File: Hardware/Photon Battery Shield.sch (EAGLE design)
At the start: 24 parts, among them U1 MAX1704X, U2 MCP73831

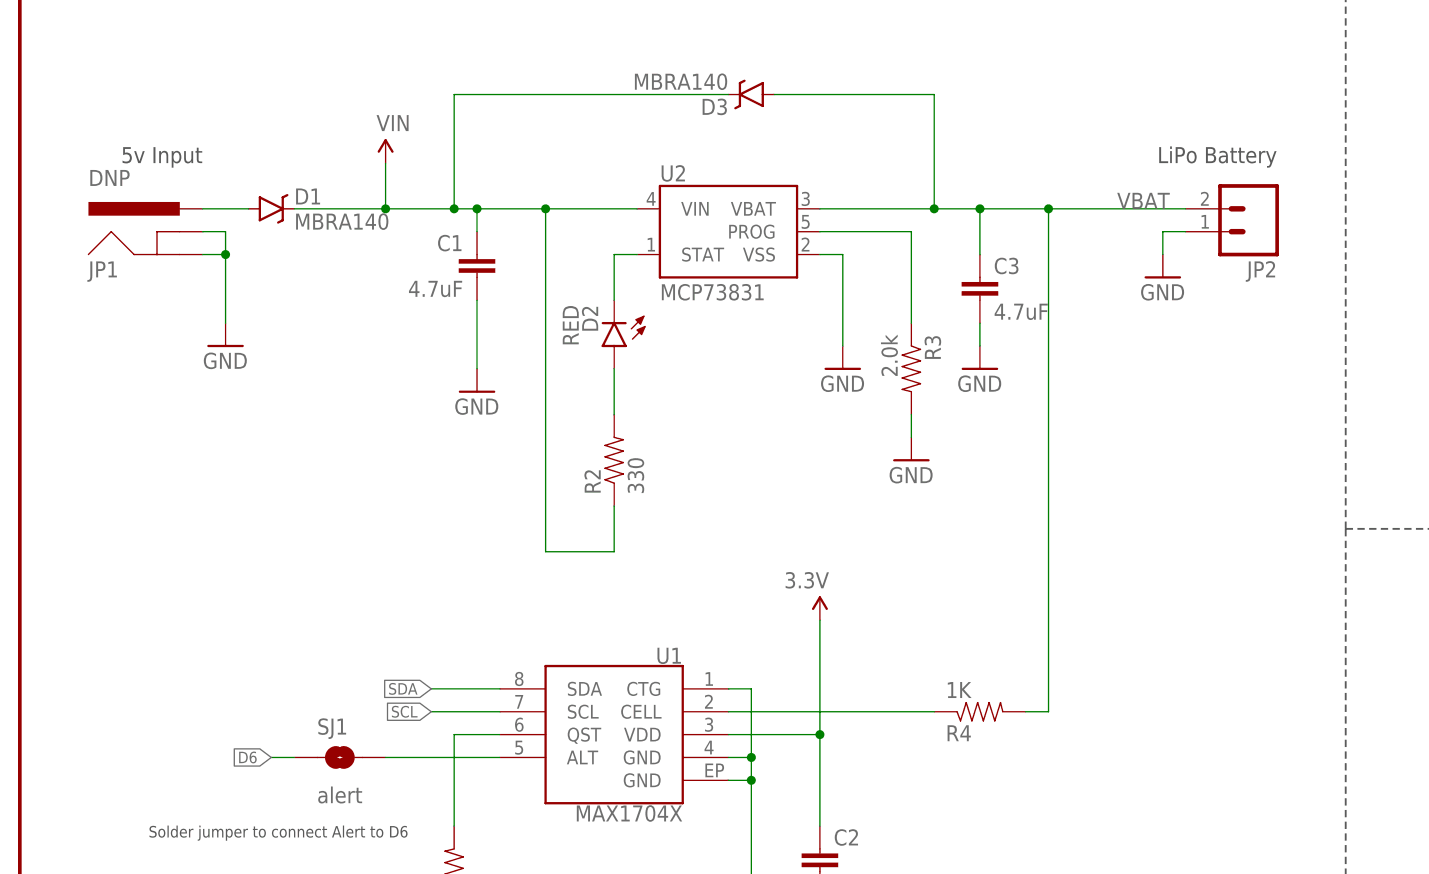
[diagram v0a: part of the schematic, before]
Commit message: Adding test point to VBAT. Reducing bSilk on barrel jack to avoid going over board.
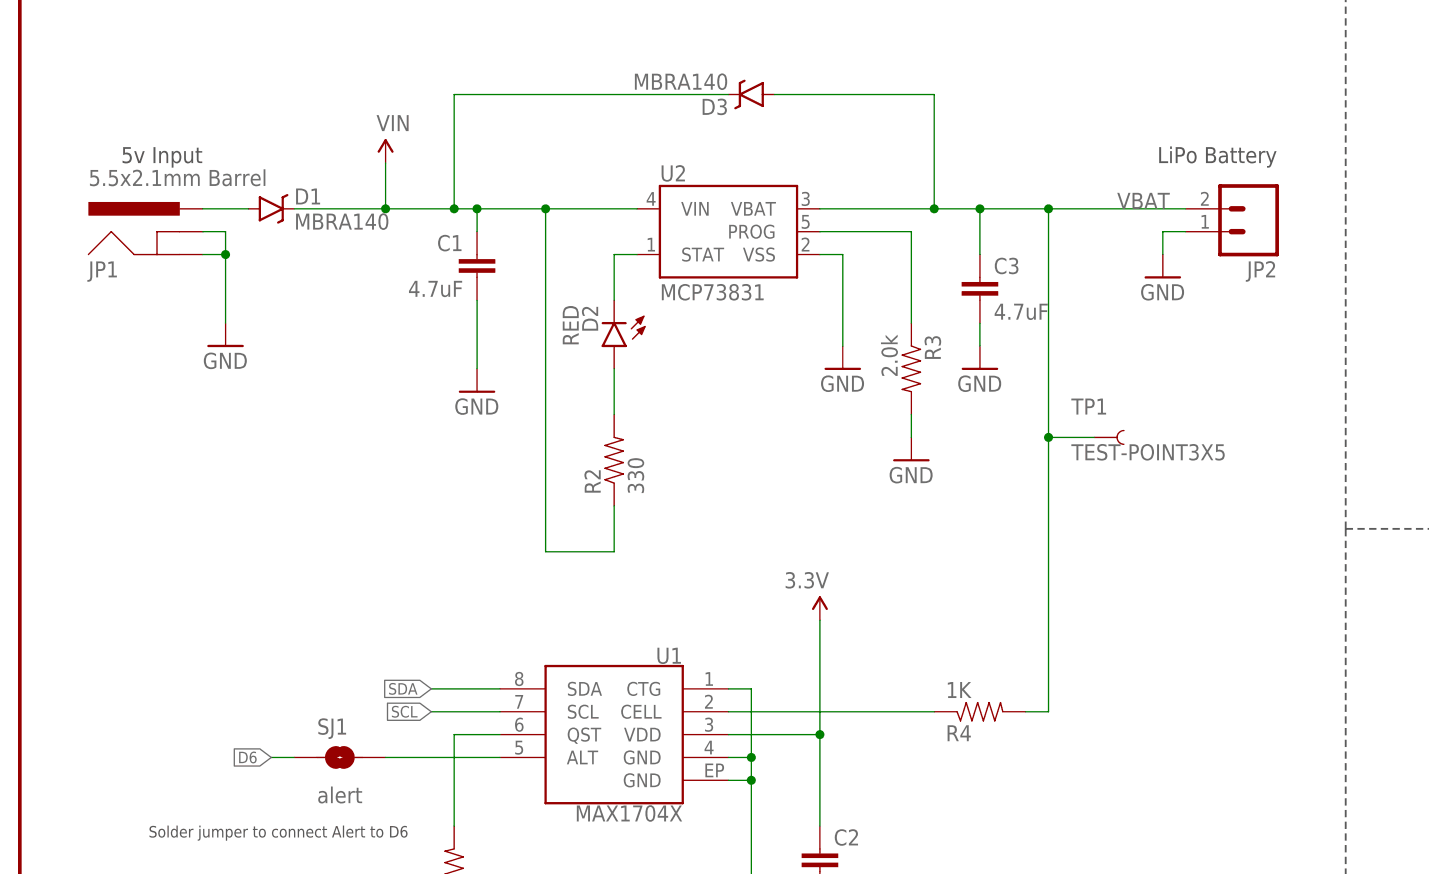
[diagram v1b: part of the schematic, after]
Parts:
- added TP1: TEST-POINT3X5, SparkFun-Passives:TEST-POINT3X5
- JP1: value DNP -> 5.5x2.1mm Barrel
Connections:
- net VBAT: now also TP1.1
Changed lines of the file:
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@@
 <part name="SUPPLY5" library="SparkFun-Aesthetics" deviceset="3.3V" device=""/>
 <part name="GND10" library="SparkFun-Aesthetics" deviceset="GND" device=""/>
-<part name="JP1" library="SparkFun-Connectors" deviceset="POWER_JACK" device="SMD" value="DNP"/>
+<part name="JP1" library="SparkFun-Connectors" deviceset="POWER_JACK" device="SMD" value="5.5x2.1mm Barrel"/>
 <part name="D1" library="SparkFun-DiscreteSemi" deviceset="DIODE-SCHOTTKY" device="-MBRA140" value="MBRA140"/>
 <part name="D3" library="SparkFun-DiscreteSemi" deviceset="DIODE-SCHOTTKY" device="-MBRA140" value="MBRA140"/>
@@
 <part name="LOGO3" library="SparkFun-Aesthetics" deviceset="SFE_LOGO_NAME_FLAME" device=".1_INCH"/>
 <part name="SJ1" library="SparkFun-Passives" deviceset="JUMPER-PAD-2-NO" device="YES_SILK" value="alert"/>
+<part name="TP1" library="SparkFun-Passives" deviceset="TEST-POINT" device="3X5"/>
 </parts>
 <sheets>
@@
 <instance part="LOGO3" gate="G$1" x="15.24" y="-12.7"/>
 <instance part="SJ1" gate="G$1" x="-7.62" y="68.58"/>
+<instance part="TP1" gate="G$1" x="76.2" y="104.14"/>
 </instances>
 <busses>
@@
 <junction x="63.5" y="129.54"/>
 <wire x1="71.12" y1="129.54" x2="63.5" y2="129.54" width="0.1524" layer="91"/>
-<wire x1="71.12" y1="129.54" x2="71.12" y2="73.66" width="0.1524" layer="91"/>
+<wire x1="71.12" y1="129.54" x2="71.12" y2="104.14" width="0.1524" layer="91"/>
 <pinref part="R4" gate="G$1" pin="2"/>
+<wire x1="71.12" y1="104.14" x2="71.12" y2="73.66" width="0.1524" layer="91"/>
 <wire x1="71.12" y1="73.66" x2="68.58" y2="73.66" width="0.1524" layer="91"/>
 <label x="78.74" y="129.54" size="1.778" layer="95"/>
@@
 <wire x1="71.12" y1="129.54" x2="86.36" y2="129.54" width="0.1524" layer="91"/>
 <junction x="71.12" y="129.54"/>
-</segment>
-</net>
+<pinref part="TP1" gate="G$1" pin="1"/>
+<wire x1="76.2" y1="104.14" x2="71.12" y2="104.14" width="0.1524" layer="91"/>
+<junction x="71.12" y="104.14"/>
+</segment>
+</net>
